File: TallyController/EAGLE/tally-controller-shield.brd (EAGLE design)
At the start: 101.6 x 53.3 mm, 27 parts, among them J2 Mega R3, U1 SN75174N, U2 SN75174N, U3 SN75174N

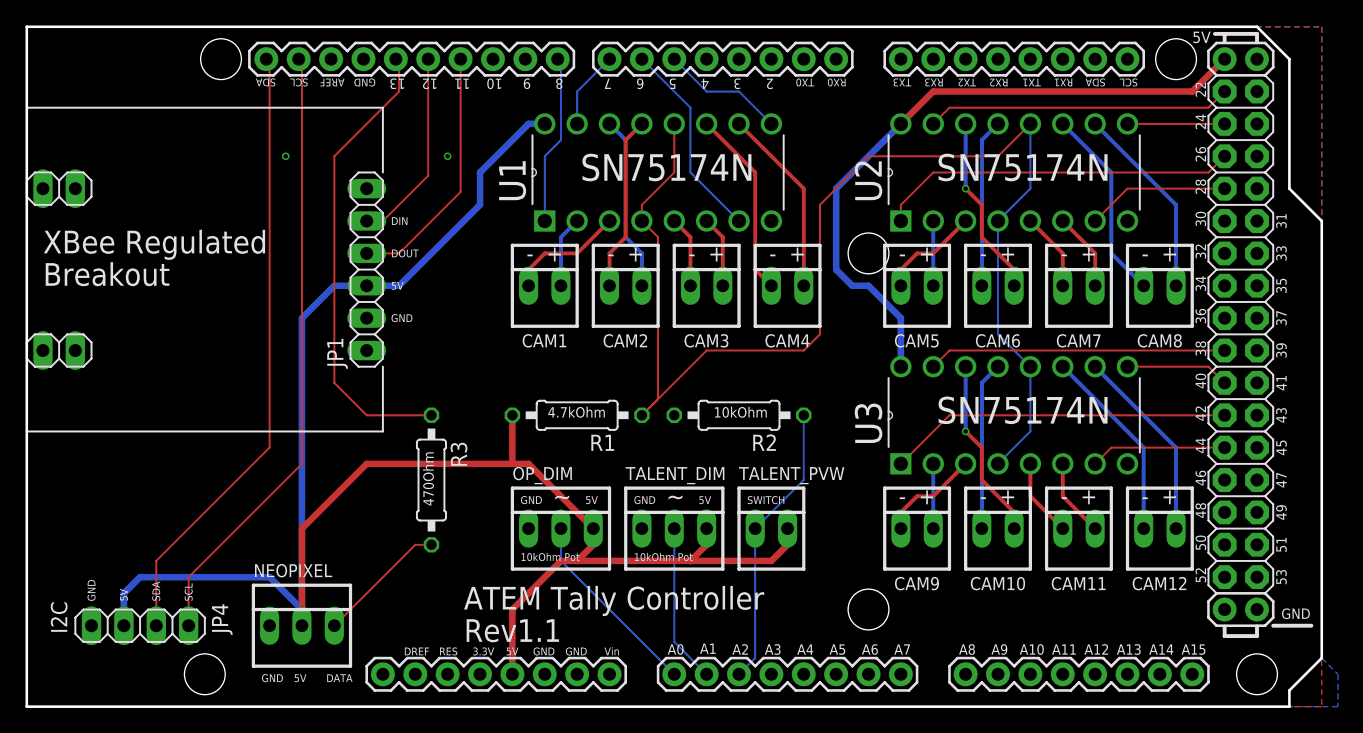
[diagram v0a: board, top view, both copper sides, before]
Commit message: Slim down some spacings to possibly use some 8 pin headers instead of 4x 2pin.  Fix hole drill sizes.
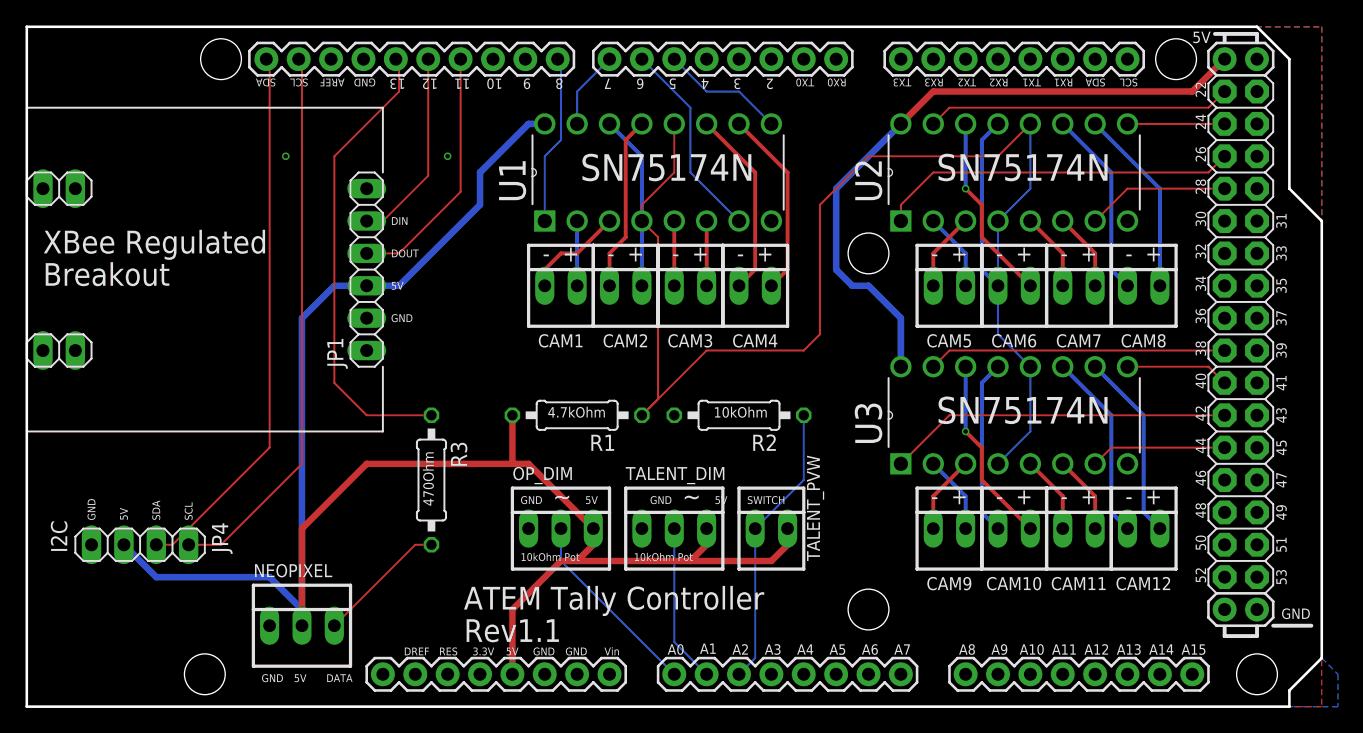
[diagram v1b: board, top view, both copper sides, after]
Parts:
- moved JP4 6.35 mm to (8.89, 12.7)
- moved CAM5 2.54 mm to (72.4, 33.0)
- moved CAM9 2.54 mm to (72.4, 14.0)
- moved CAM4 2.54 mm to (57.1, 33.0)
- moved CAM12 1.27 mm to (87.6, 14.0)
- moved CAM8 1.27 mm to (87.6, 33.0)
- moved CAM3 1.27 mm to (52.1, 33.0)
- moved CAM1 1.27 mm to (41.9, 33.0)
- moved CAM10 1.27 mm to (77.5, 14.0)
- moved CAM6 1.27 mm to (77.5, 33.0)
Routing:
- net MEGASDA1: track 48.2 -> 42.6 mm
- net MEGASCL1: track 48.2 -> 43.4 mm
- net 5V@0: track 143.7 -> 141.7 mm
- net CAM9D-: track 7.93 -> 6.13 mm
- net CAM5D-: track 7.93 -> 6.13 mm
- net CAM1D-: track 9.20 -> 7.93 mm
- net CAM9D+: track 5.08 -> 6.13 mm
- net CAM5D+: track 5.08 -> 6.13 mm
- net CAM3D-: track 5.61 -> 5.08 mm
- net CAM1D+: track 5.61 -> 5.08 mm
- net CAM6D-: track 13.2 -> 13.8 mm
- net CAM12D+: track 15.3 -> 14.8 mm
- net CAM10D-: track 13.2 -> 13.8 mm
- net CAM8D-: track 15.3 -> 14.8 mm
- net CAM8D+: track 15.3 -> 14.8 mm
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
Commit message: Add external power input to power all the external bits.  Fix DRC errors that I didn't catch for some reason.
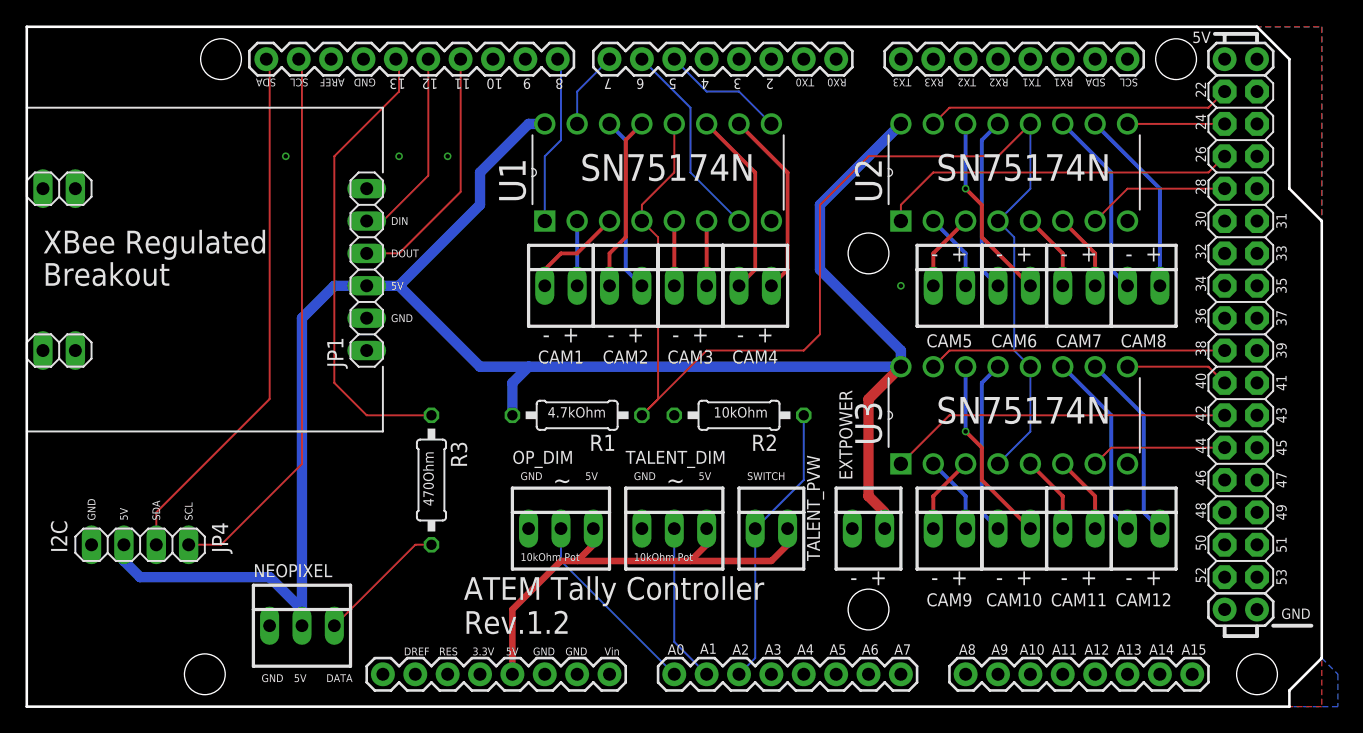
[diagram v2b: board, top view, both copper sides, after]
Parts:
- added EXTPOWER: 22-23-2021, con-molex:22-23-2021
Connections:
- new net VCC: EXTPOWER.2, JP1.3, JP4.2, NEOPIXEL.2, R1.2, U1.16, U2.16, U3.16
- net 5V@0: no longer JP1.3, JP4.2, NEOPIXEL.2, R1.2, U1.16
- net 5V@1: no longer U2.16, U3.16
- net GND: now also EXTPOWER.1
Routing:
- net VCC: track 0.00 -> 152.7 mm
- net 5V@0: track 141.7 -> 36.2 mm
- net 5V@1: track 51.5 -> 0.00 mm
- net MEGASDA1: track 42.6 -> 41.9 mm
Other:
- board text added: "ATEM Tally Controller Rev.1.2"
- board text removed: "ATEM Tally Controller"
- board text removed: "Rev1.1"
